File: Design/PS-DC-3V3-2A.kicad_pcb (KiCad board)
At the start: 2 copper layers, 24.1 x 11.4 mm, 13 parts, among them J1 Conn_01x02, J2 Conn_01x04, U1 MAX17643

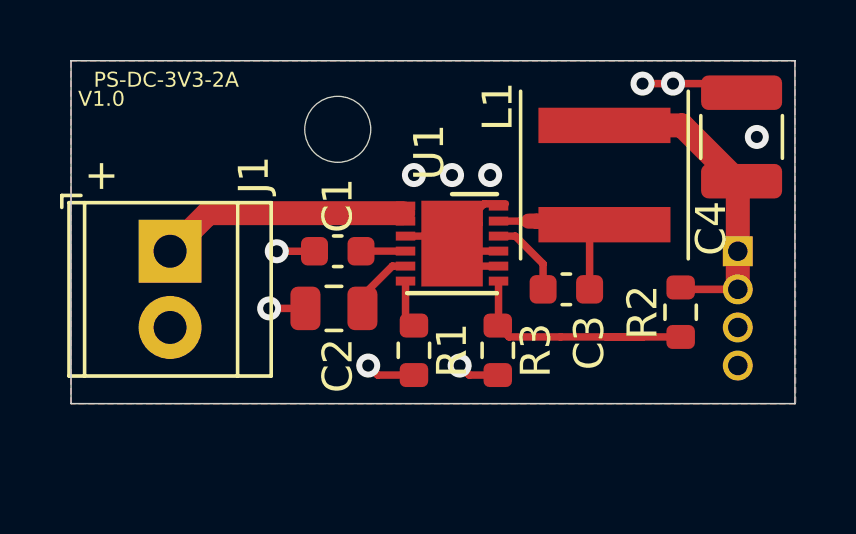
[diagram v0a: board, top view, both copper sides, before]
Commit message: Add Sync and reset components, re-arange
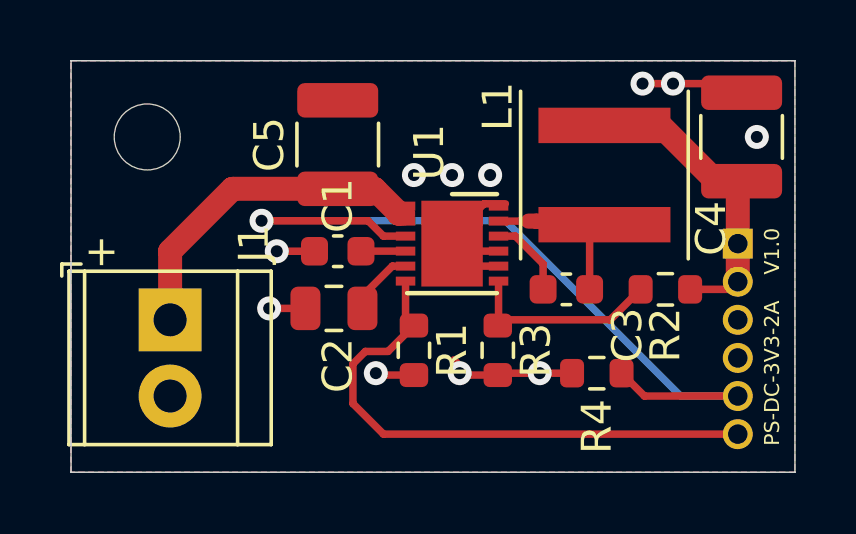
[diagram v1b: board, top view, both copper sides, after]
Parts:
- removed REF**: OSHW-Logo2_7.3x6mm_SilkScreen, Symbol:OSHW-Logo2_7.3x6mm_SilkScreen
- removed REF**: MountingHole_2.2mm_M2, MountingHole:MountingHole_2.2mm_M2
- added C5: 2.2u, Capacitor_SMD:C_1210_3225Metric, F.Cu at (144.8, 96.8)
- added MP0: MountingHole_2.2mm_M2, MountingHole:MountingHole_2.2mm_M2, F.Cu at (138.4, 96.5)
- added R4: 40.2k, Resistor_SMD:R_0603_1608Metric, F.Cu at (153.4, 104.4)
- J2: footprint Connector_PinHeader_1.27mm:PinHeader_1x04_P1.27mm_Vertical -> Connector_PinHeader_1.27mm:PinHeader_1x06_P1.27mm_Vertical
- moved J1 2.29 mm to (139.2, 102.6)
- moved R2 0.92 mm to (155.7, 101.6), turned to 180 degrees
- moved J2 0.25 mm to (158.1, 100.1)
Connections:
- R1 pad 1: Net-(R1-Pad1) -> SYNC
- U1 pad 3: GND -> \Reset
- U1 pad 6: Net-(R1-Pad1) -> SYNC
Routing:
- net \Reset: track 0.00 -> 27.9 mm, vias 0 -> 1
- net SYNC: track 0.00 -> 18.9 mm
- net Net-(R2-Pad2): track 9.49 -> 7.21 mm
- net Vin: track 8.80 -> 10.8 mm
- net Net-(R1-Pad1): track 1.81 -> 0.00 mm
- net GND: track 17.6 -> 18.7 mm, vias 10 -> 11
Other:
- board size 24.1 x 11.4 mm -> 24.1 x 13.7 mm
- board text added: "SYNC"
- board text added: "\RESET"

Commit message: Change Con_1x04 => Con_1x06
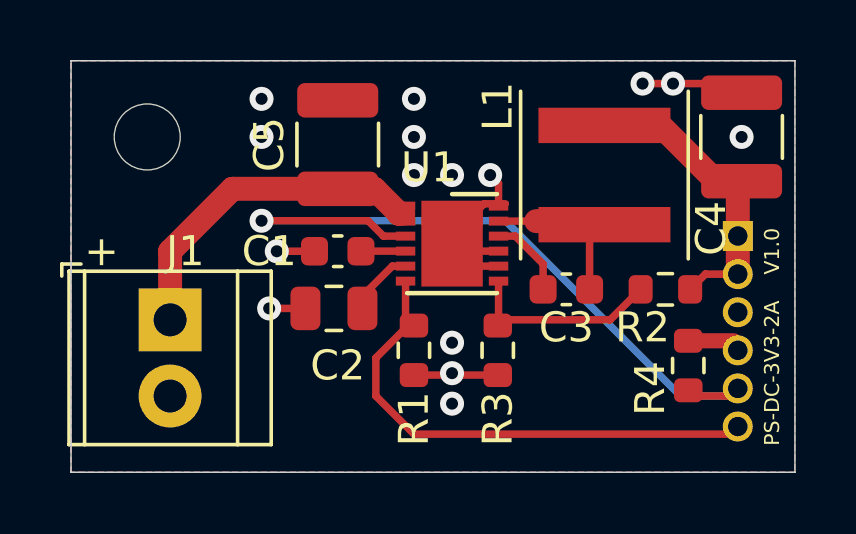
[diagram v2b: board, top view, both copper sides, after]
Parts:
- J2: value Conn_01x04 -> Conn_01x06
- moved R4 3.06 mm to (156.5, 104.1), turned to 90 degrees
- moved J2 0.25 mm to (158.1, 99.8)
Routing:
- net \Reset: track 27.9 -> 25.2 mm
- net SYNC: track 18.9 -> 17.4 mm
- net Net-(C3-Pad2): track 6.33 -> 5.56 mm
- net GND: track 18.7 -> 18.9 mm, vias 11 -> 15

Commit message: Suppress pull-down resistaor on nReset signal, replaced by 10k pull-up
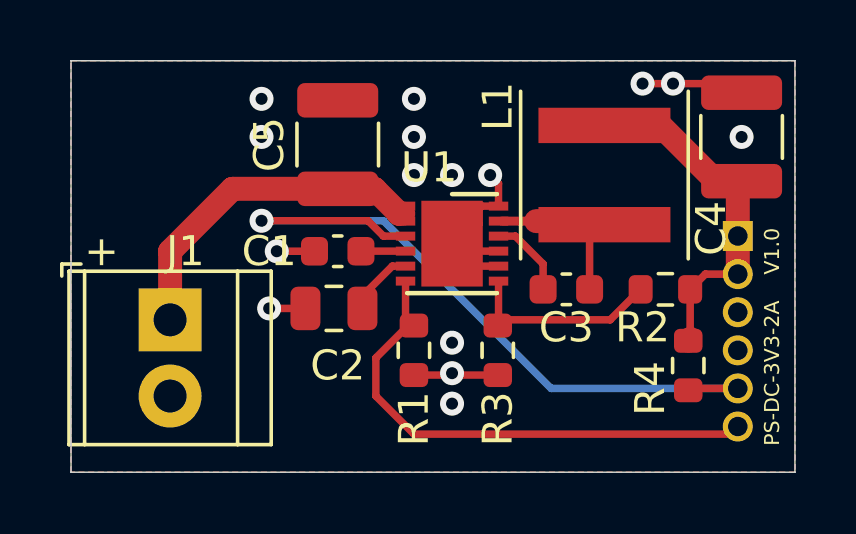
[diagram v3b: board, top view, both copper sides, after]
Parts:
- removed MP0: MountingHole_2.2mm_M2, MountingHole:MountingHole_2.2mm_M2
- R4: value 40.2k -> 10k
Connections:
- R4 pad 2: GND -> Vout
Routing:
- net GND: track 18.9 -> 17.1 mm
- net Vout: track 11.2 -> 12.9 mm

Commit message: M2 mounting hole added
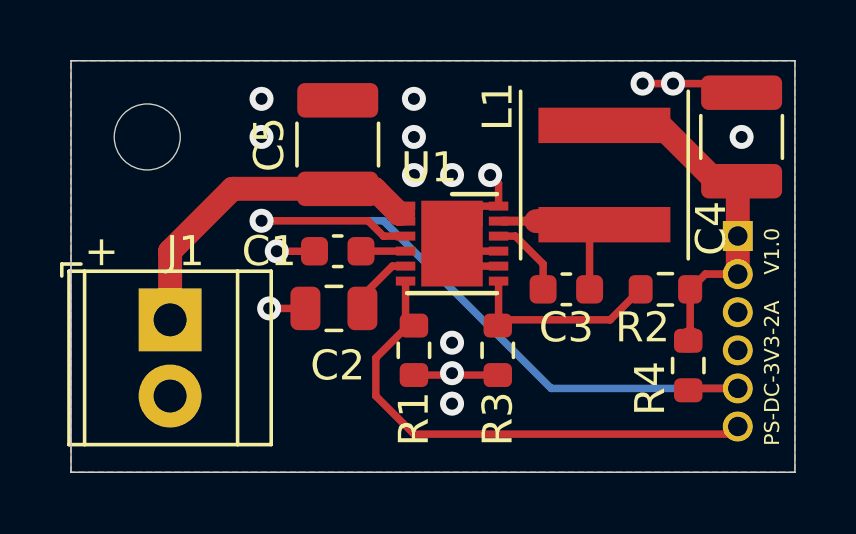
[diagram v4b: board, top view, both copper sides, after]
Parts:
- added REF**: MountingHole_2.2mm_M2, MountingHole:MountingHole_2.2mm_M2, F.Cu at (138.4, 96.5)
